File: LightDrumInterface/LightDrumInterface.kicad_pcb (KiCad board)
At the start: 2 copper layers, 151 x 83 mm, 62 parts, among them J1 Conn_01x04_Male, J2 DEBUG-CONN, J3 Conn_01x04_Male, J4 B24B-PHDSS(LF)(SN), J5 B24B-PHDSS(LF)(SN), SW1 RESET-SW, U1 STP16CP05, U2 TPL0401B-10-Q1, U3 74AUP2G04, U4 PC817

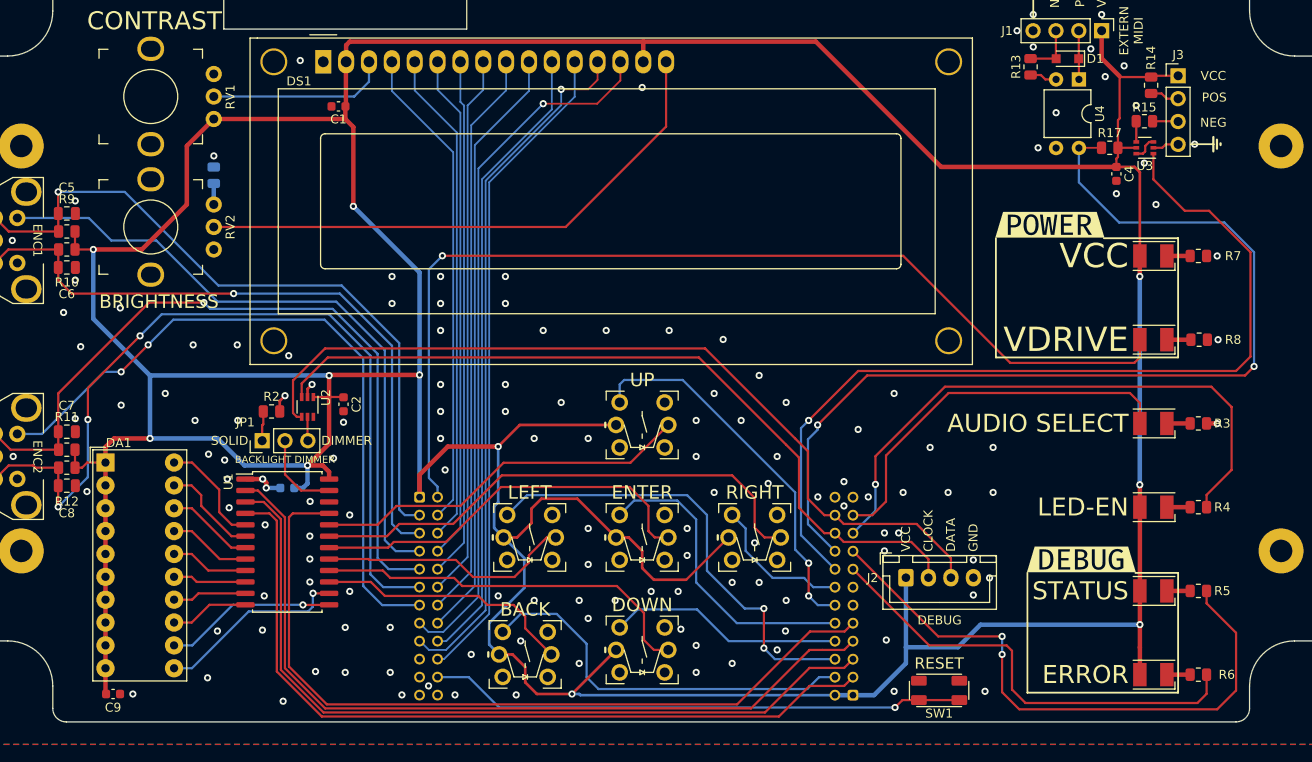
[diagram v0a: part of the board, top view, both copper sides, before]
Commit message: Replace interface harnesses with FPC cable
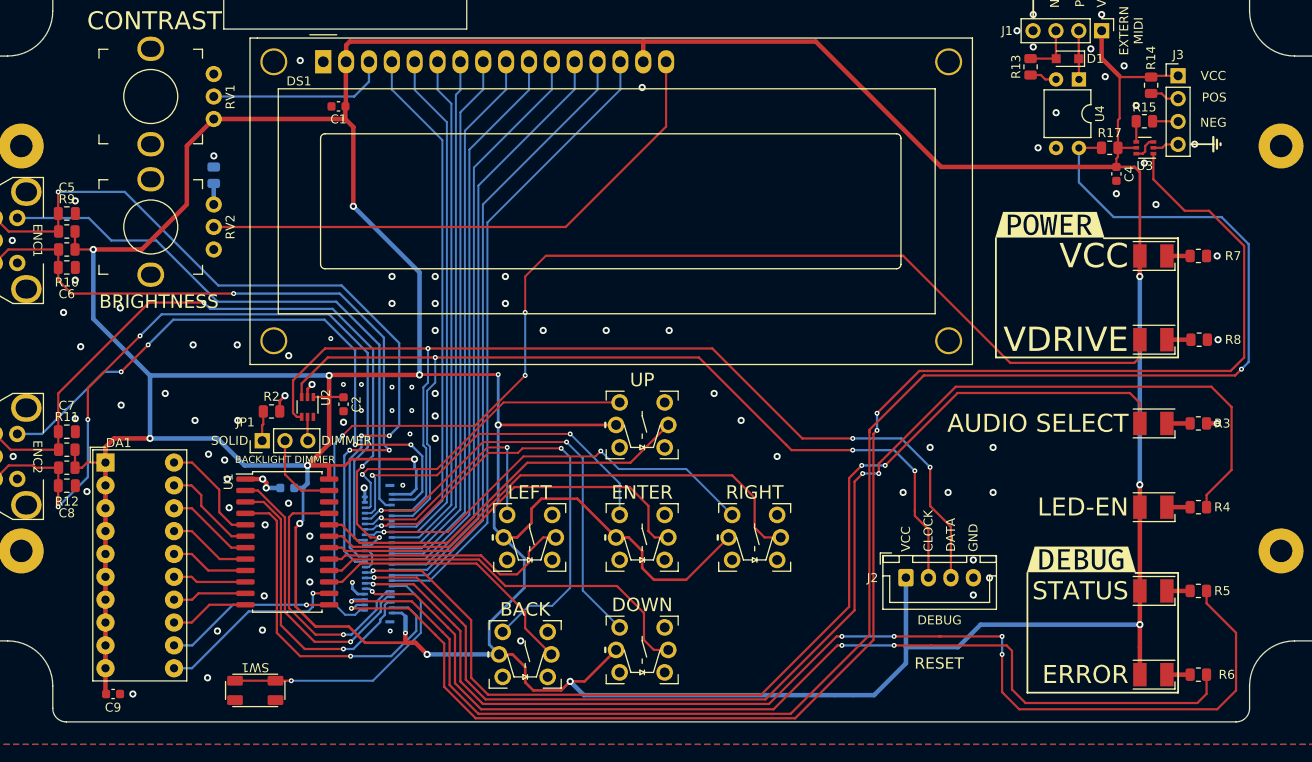
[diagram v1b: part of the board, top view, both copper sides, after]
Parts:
- removed J4, J5: B24B-PHDSS(LF)(SN), Daxxn_Connectors:B24B-PHDSS(LF)(SN)
- added J-INTERFACE1: INTERFACE CONN, Daxxn_Connectors:5025984593, B.Cu at (75.2, 92.8)
- C1, C2, C3, C4, C5, C6, C7, C8: value ${D-CAP} -> 100nF
- R1: value 120${R} -> 120Ω
- R10, R11, R12, R17, R9: value ${P-RES} -> 10KΩ
- R13, R14, R15: value 220${R} -> 220Ω
- R2: value 500${R} -> 560Ω
- R3, R4, R6: value ${LED-RES} -> 330Ω
- R5: value ${LED-RES} -> 470Ω
- R7: value 510${R} -> 3KΩ
- R8: value 1K${R} -> 5.6KΩ
- RV1: value 10K${R} -> 10KΩ
- RV2: value 1K${R} -> 1KΩ
- moved SW1 76.0 mm to (60.0, 108.0), turned to 180 degrees
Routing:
- net /DIAG-AUDIO-SEL: track 43.2 -> 120.7 mm, vias 0 -> 3
- net /DIAG-STRIP-EN: track 65.6 -> 142.0 mm, vias 1 -> 3
- net /MIDI-IN: track 108.6 -> 180.1 mm
- net /MIDI-OUT: track 99.1 -> 168.4 mm, vias 1 -> 3
- net /DIAG-DEBUG: track 50.5 -> 112.9 mm, vias 0 -> 3
- net /DIAG-STATUS: track 66.8 -> 129.0 mm, vias 2 -> 5
- net /IND-~{OE}: track 89.4 -> 29.9 mm, vias 0 -> 1
- net /IND-SDATA: track 90.5 -> 32.0 mm, vias 0 -> 1
- net /IND-CLK: track 89.5 -> 32.9 mm, vias 0 -> 1
- net /IND-LE: track 88.5 -> 38.8 mm, vias 0 -> 1
- net VCC: track 585.8 -> 635.4 mm, vias 11 -> 16
- net /MENU-RIGHT: track 16.2 -> 47.6 mm, vias 0 -> 2
- net /~{RESET}: track 59.7 -> 30.4 mm
- net /MENU-LEFT: track 51.1 -> 27.0 mm
- net /I2C-SCLK: track 87.0 -> 109.9 mm, vias 0 -> 3
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
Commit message: Add docs and gerbers for REV7
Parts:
- H4: value M2.5 -> locked
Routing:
- net Vdrive: track 133.6 -> 123.1 mm
- net /I2C-SDA: track 117.0 -> 119.4 mm
- net /MIDI-IN: track 180.1 -> 178.3 mm
- net /DIAG-AUDIO-SEL: track 120.7 -> 121.6 mm
- net /DIAG-STRIP-EN: track 142.0 -> 142.8 mm
- net /MIDI-OUT: track 168.4 -> 168.2 mm, vias 3 -> 1
- net GND: vias 93 -> 95

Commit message: Add logo to interface PCB
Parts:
- added G***: LOGO, Daxxn_Logos_Art:LightDrum_Logo2_Cu_Spoke, F.Cu at (132.5, 89.5)
- added G***: LOGO, Daxxn_Logos_Art:LightDrum_Logo2, F.Cu at (132.5, 89.5)
- moved J2 9.89 mm to (128.8, 104.7)
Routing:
- net /I2C-SDA: track 119.4 -> 129.3 mm
- net /DIAG-STATUS: track 129.0 -> 119.2 mm, vias 5 -> 3
- net /I2C-SCLK: track 110.0 -> 119.5 mm
- net /MIDI-IN: track 178.3 -> 187.4 mm
- net /MIDI-OUT: track 168.2 -> 177.2 mm
- net /DIAG-STRIP-EN: track 142.8 -> 150.7 mm
- net /DIAG-AUDIO-SEL: track 121.6 -> 129.4 mm
- net /DIAG-DEBUG: track 112.7 -> 107.5 mm
- net VCC: track 635.3 -> 632.7 mm
- net /MENU-LEFT: track 27.0 -> 25.6 mm
- net GND: vias 95 -> 114
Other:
- board text added: "LIGHT DRUM"
- board text added: "REV7"

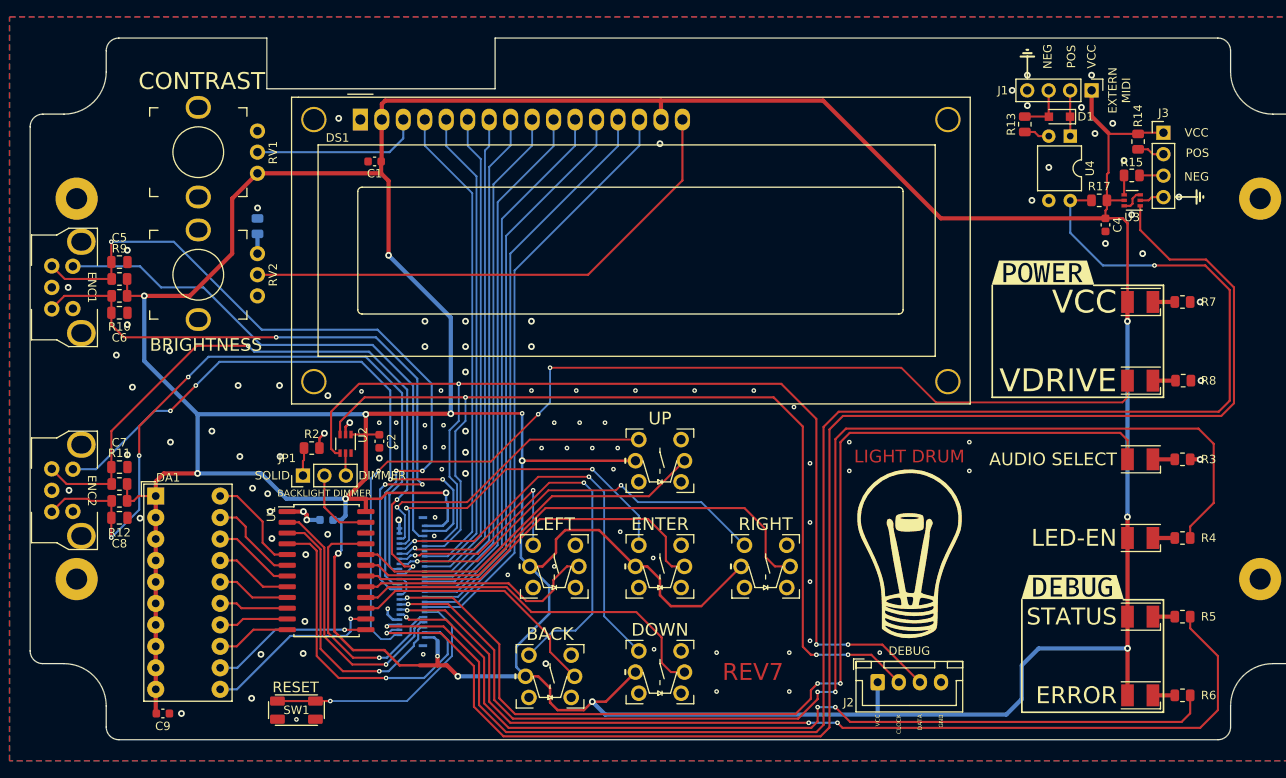
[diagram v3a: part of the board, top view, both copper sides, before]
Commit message: Replaced display and FPC cable
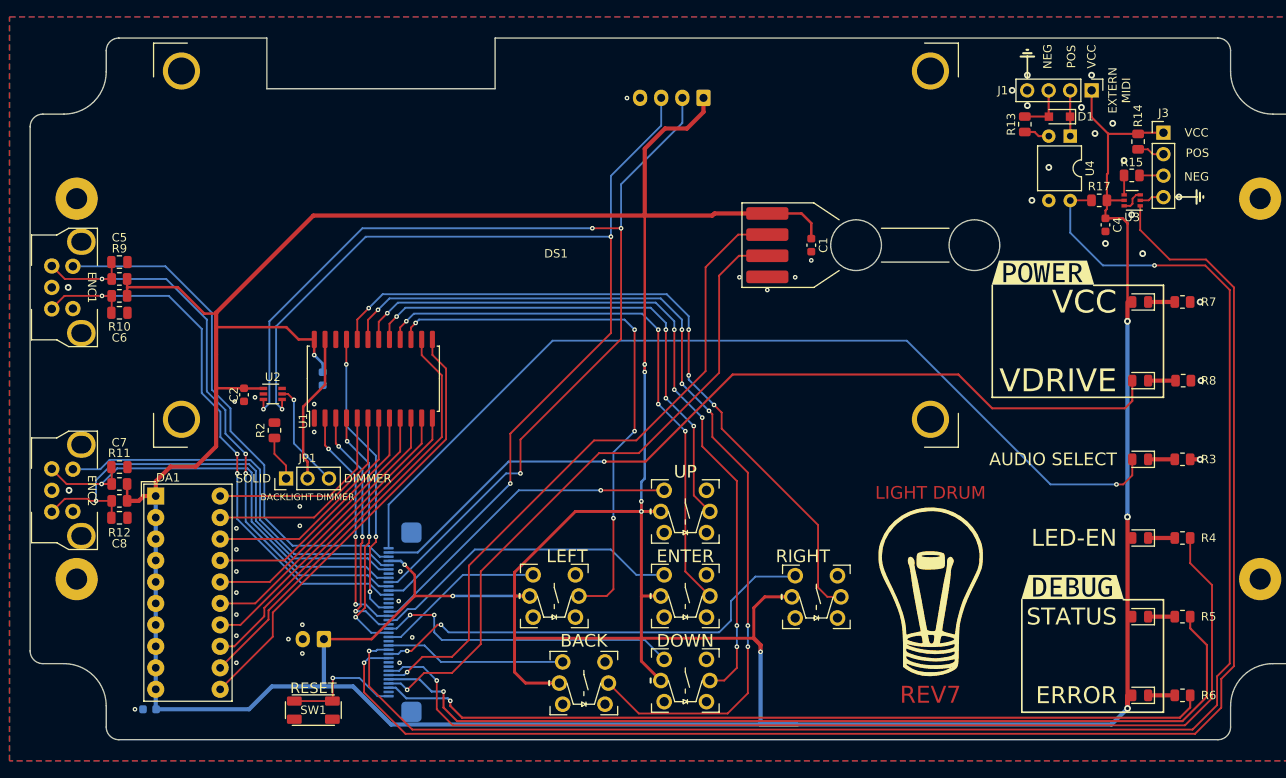
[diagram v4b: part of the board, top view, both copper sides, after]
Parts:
- removed J-INTERFACE1: INTERFACE CONN, Daxxn_Connectors:5025984593
- removed R1: 120Ω, Resistor_SMD:R_0805_2012Metric
- removed RV1: 10KΩ, Daxxn_Switches:PT01-D120K2-B103
- removed RV2: 1KΩ, Daxxn_Switches:PT01-D120K2-B103
- added J4: PWR-CONN, Connector_JST:JST_XA_B02B-XASK-1_1x02_P2.50mm_Vertical, B.Cu at (63.2, 99.6)
- added J6: 0541323662, Daxxn_Connectors:0541323662, B.Cu at (70.9, 97.6)
- C9, J2: moved to B.Cu
- D-AUDIO-SEL1, D-DBG1, D-STA1, D-STRIP-EN1, D-VCC1, D-VDRIVE1: footprint Daxxn_LEDs:LED_PLCC-2 -> LED_SMD:LED_0805_2012Metric
- DS1: value WC1602A -> NX4024T032; footprint Display:WC1602A -> Daxxn_Displays:NX4024T032_10mm_Harness
- moved J2 72.1 mm to (108.2, 35.6), turned to 180 degrees
- moved C1 52.6 mm to (120.9, 53.0), turned to -90 degrees
- moved DS1 27.5 mm to (90.7, 53.0), turned to -90 degrees
- moved U1 23.4 mm to (69.1, 68.8), turned to 90 degrees
- moved C2 16.9 mm to (53.8, 70.7)
- moved C3 16.7 mm to (63.1, 68.8), turned to -90 degrees
- moved U2 10.4 mm to (57.2, 70.6), turned to 0 degrees
- moved S-RGT1 7.00 mm to (121.5, 94.6)
- moved S-UP1 6.71 mm to (106.0, 84.5)
- moved G*** 5.15 mm to (135.0, 94.0) (x2)
- moved R2 4.88 mm to (57.4, 74.9), turned to 90 degrees
- moved S-ACT1 4.61 mm to (106.0, 94.5)
- moved S-BCK1 4.08 mm to (94.0, 104.8)
- moved S-LFT1 3.50 mm to (90.5, 94.5)
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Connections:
- net /I2C-SCLK renamed I2C-SCLK
- net /I2C-SDA renamed I2C-SDA
- D-AUDIO-SEL1 pad 2: /DIAG-AUDIO-SEL -> /AUDIO-RELAY
- DA1 pad 11: Net-(DA1-Pad11) -> Net-(U1-Pad13)
- DA1 pad 12: Net-(DA1-Pad12) -> Net-(U1-Pad14)
- DS1 pad 1: GND -> VCC
- DS1 pad 2: VCC -> /SCR-TX
- DS1 pad 3: Net-(DS1-Pad3) -> /SCR-RX
- DS1 pad 4: /SCR-RS -> GND
- R4 pad 2: /DIAG-STRIP-EN -> /STRIP-PWR
- S-ACT1 pad 6: Net-(S-ACT1-Pad6) -> Net-(U1-Pad16)
- S-BCK1 pad 6: Net-(S-BCK1-Pad6) -> Net-(U1-Pad19)
- S-DWN1 pad 6: Net-(S-DWN1-Pad6) -> Net-(U1-Pad18)
- S-RGT1 pad 6: Net-(S-RGT1-Pad6) -> Net-(U1-Pad20)
- S-UP1 pad 6: Net-(S-UP1-Pad6) -> Net-(U1-Pad17)
- SW1 pad 2: /~{RESET} -> ~{RESET}
- U1 pad 13: Net-(DA1-Pad12) -> Net-(U1-Pad13)
- U1 pad 14: Net-(DA1-Pad11) -> Net-(U1-Pad14)
- U1 pad 15: Net-(S-BCK1-Pad6) -> Net-(S-LFT1-Pad6)
- U1 pad 16: Net-(S-DWN1-Pad6) -> Net-(U1-Pad16)
- U1 pad 17: Net-(S-LFT1-Pad6) -> Net-(U1-Pad17)
- U1 pad 18: Net-(S-ACT1-Pad6) -> Net-(U1-Pad18)
- U1 pad 19: Net-(S-RGT1-Pad6) -> Net-(U1-Pad19)
- U1 pad 2: /IND-SDATA -> /GRAPH-SDI
- U1 pad 20: Net-(S-UP1-Pad6) -> Net-(U1-Pad20)
- U1 pad 21: /IND-~{OE} -> /GRAPH-~{OE}
- U1 pad 3: /IND-CLK -> /GRAPH-CLK
- U1 pad 4: /IND-LE -> /GRAPH-LE
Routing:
- net /DIAG-STRIP-EN: track 150.7 -> 0.00 mm, vias 3 -> 0
- net /DIAG-AUDIO-SEL: track 129.4 -> 0.00 mm, vias 3 -> 0
- net /STRIP-PWR: track 0.00 -> 123.8 mm, vias 0 -> 1
- net /AUDIO-RELAY: track 0.00 -> 110.5 mm, vias 0 -> 1
- net Net-(U1-Pad19): track 0.00 -> 108.0 mm, vias 0 -> 6
- net Net-(U1-Pad18): track 0.00 -> 86.8 mm, vias 0 -> 6
- net Net-(U1-Pad20): track 0.00 -> 85.5 mm, vias 0 -> 4
- net /SCR-TX: track 0.00 -> 78.7 mm, vias 0 -> 1
- net /SCR-RX: track 0.00 -> 78.2 mm, vias 0 -> 1
- net /SCR-D7: track 70.7 -> 0.00 mm
- net /SCR-D6: track 68.9 -> 0.00 mm
- net Net-(U1-Pad16): track 0.00 -> 67.4 mm, vias 0 -> 4
- net /SCR-D5: track 67.2 -> 0.00 mm
- net /SCR-D4: track 65.5 -> 0.00 mm
- net /SCR-D3: track 63.8 -> 0.00 mm
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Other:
- board text removed: "BRIGHTNESS"
- board text removed: "CONTRAST"

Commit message: Replace with smaller case (WIP)
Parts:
- removed H1, H2, H3: M2.5, MountingHole:MountingHole_2.5mm_Pad
- removed H4: locked, MountingHole:MountingHole_2.5mm_Pad
- removed the REF** at (104.0, 70.0)
- added REF**: LeMotech_Black_ENC-115x90, Daxxn_Enclosures:LeMotech_Black_ENC-115x90, F.Cu at (0.00, 0.00)
- moved R6 220.4 mm to (-6.00, -33.0), turned to -90 degrees
- moved D-DBG1 219.8 mm to (-6.00, -38.0), turned to 90 degrees
- moved R5 208.5 mm to (1.80, -33.0), turned to -90 degrees
- moved D-STA1 207.8 mm to (1.80, -38.0), turned to 90 degrees
- moved R4 196.6 mm to (9.60, -33.0), turned to -90 degrees
- moved D-STRIP-EN1 195.8 mm to (9.60, -38.0), turned to 90 degrees
- moved kibuzzard-62EEA0C0 189.5 mm to (5.50, -27.0)
- moved R3 184.7 mm to (17.4, -33.0), turned to -90 degrees
- moved D-AUDIO-SEL1 183.9 mm to (17.4, -38.0), turned to 90 degrees
- moved G*** 176.6 mm to (-30.0, 31.0) (x2)
- moved R8 172.9 mm to (25.2, -32.9), turned to -90 degrees
- moved D-VDRIVE1 172.0 mm to (25.2, -38.0), turned to 90 degrees
- moved C9 162.4 mm to (-33.5, -35.5), turned to -90 degrees
- moved R7 161.2 mm to (33.0, -33.0), turned to -90 degrees
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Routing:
- net VCC: track 584.7 -> 0.00 mm, vias 11 -> 0
- net /MIDI-IN: track 187.9 -> 0.00 mm, vias 2 -> 0
- net /MIDI-OUT: track 178.4 -> 0.00 mm, vias 1 -> 0
- net I2C-SCLK: track 131.3 -> 0.00 mm, vias 4 -> 0
- net I2C-SDA: track 127.9 -> 0.00 mm, vias 3 -> 0
- net /STRIP-PWR: track 123.8 -> 0.00 mm, vias 1 -> 0
- net /DIAG-STATUS: track 111.4 -> 0.00 mm, vias 1 -> 0
- net /AUDIO-RELAY: track 110.5 -> 0.00 mm, vias 1 -> 0
- net Net-(U1-Pad19): track 108.0 -> 0.00 mm, vias 6 -> 0
- net Vdrive: track 101.1 -> 0.00 mm, vias 1 -> 0
- net /DIAG-DEBUG: track 98.6 -> 0.00 mm, vias 1 -> 0
- net Net-(U1-Pad18): track 86.8 -> 0.00 mm, vias 6 -> 0
- net Net-(U1-Pad20): track 85.5 -> 0.00 mm, vias 4 -> 0
- net /SCR-TX: track 78.7 -> 0.00 mm, vias 1 -> 0
- net /SCR-RX: track 78.2 -> 0.00 mm, vias 1 -> 0
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- removed copper zone on B.Cu, net GND
- removed copper zone on F.Cu, net GND
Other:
- board size 151 x 83 mm -> 108 x 83 mm
- board text added: "REV8"
- board text removed: "REV7"

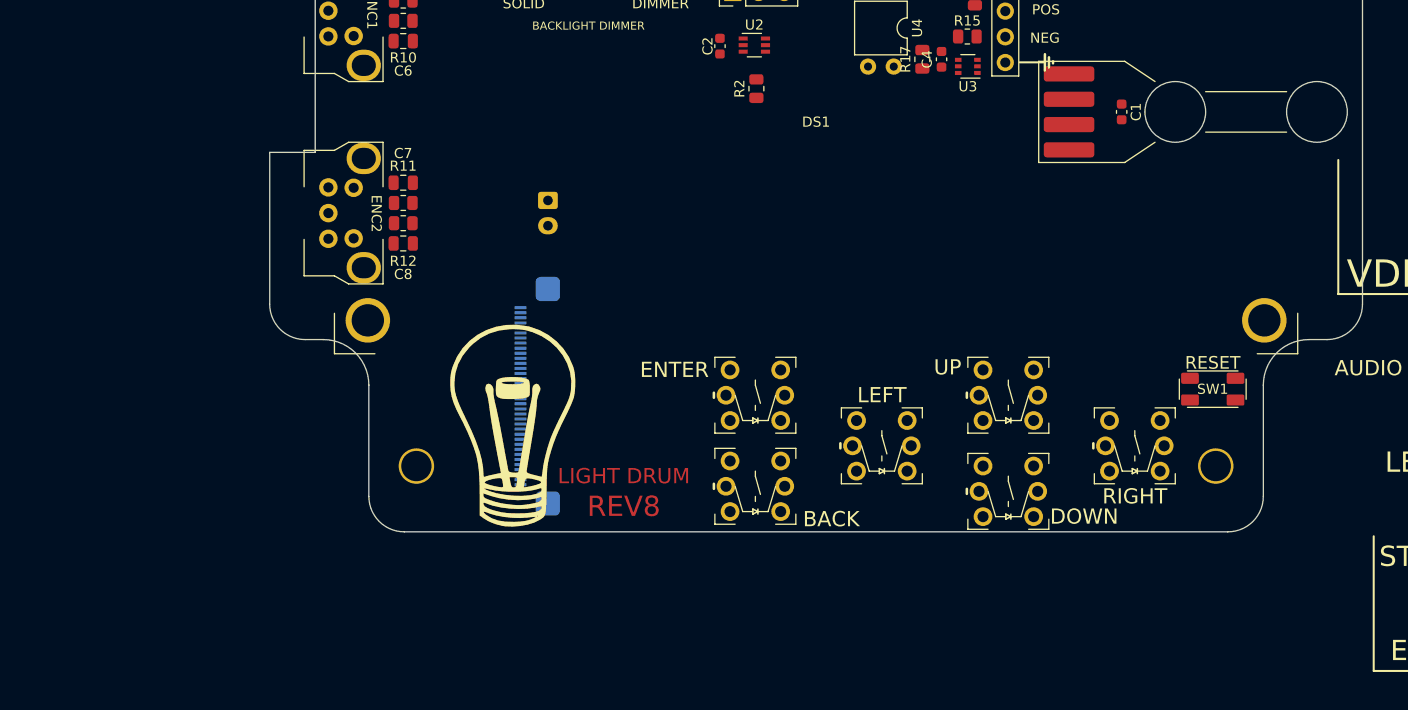
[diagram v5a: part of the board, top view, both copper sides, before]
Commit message: Simplify analog power supply and add some routing
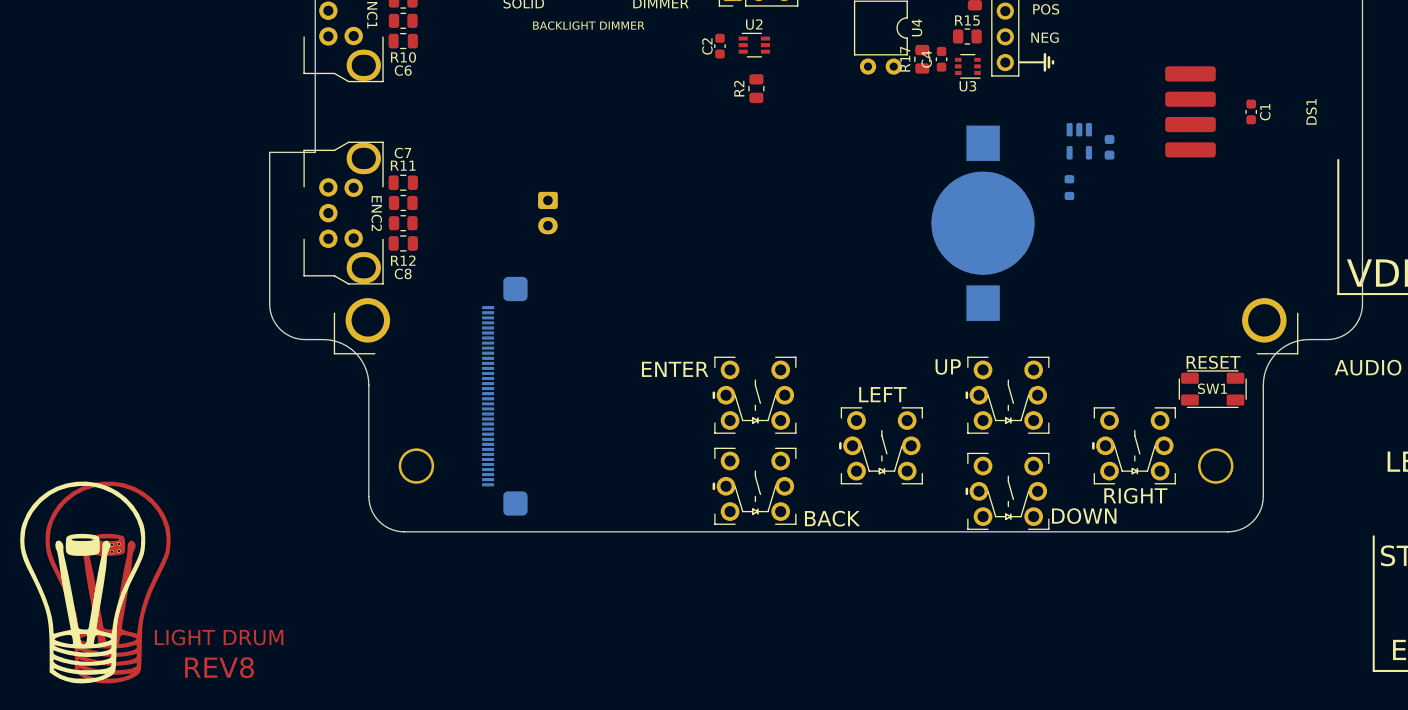
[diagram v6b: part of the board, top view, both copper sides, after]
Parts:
- added BAT101: 12mm COIN, Battery:BatteryHolder_Keystone_3000_1x12mm, B.Cu at (16.5, 11.0)
- added C101: 100nF, Capacitor_SMD:C_0603_1608Metric, B.Cu at (29.0, 3.50)
- added R101: 1.2K, Resistor_SMD:R_0603_1608Metric, B.Cu at (25.0, 7.48)
- added U101: LTC4054ES5-4.2, Package_TO_SOT_SMD:TSOT-23-5, B.Cu at (26.0, 2.90)
- DS1: footprint Daxxn_Displays:NX4024T032_10mm_Harness -> Daxxn_Displays:NX4024T032_10mm
- moved G*** 45.2 mm to (-72.5, 46.5)
- moved G*** 42.9 mm to (-70.0, 46.5)
- moved C1 12.8 mm to (43.0, 0.00)
- moved J6 3.20 mm to (-32.4, 28.1)
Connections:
- C2 pad 1: VCC -> VDD
- C3 pad 1: VCC -> VDD
- C9 pad 1: VCC -> VDD
- D-DBG1 pad 2: VCC -> VDD
- D-STA1 pad 2: VCC -> VDD
- D-STRIP-EN1 pad 2: VCC -> VDD
- D-VCC1 pad 2: VCC -> VDD
- DA1 pad 1: VCC -> VDD
- DA1 pad 10: VCC -> VDD
- DA1 pad 2: VCC -> VDD
- DA1 pad 3: VCC -> VDD
- DA1 pad 4: VCC -> VDD
- DA1 pad 5: VCC -> VDD
- DA1 pad 6: VCC -> VDD
- DA1 pad 7: VCC -> VDD
- DA1 pad 8: VCC -> VDD
- DA1 pad 9: VCC -> VDD
- J6 pad 13: GND -> VCC
- J6 pad 14: GND -> /VBAT
- J6 pad 23: GND -> /CHARGE-STATUS
- J6 pad 35: GND -> VDD
- J6 pad 4: VCC -> VDD
- R10 pad 1: VCC -> VDD
- R11 pad 2: VCC -> VDD
- R12 pad 1: VCC -> VDD
- R9 pad 2: VCC -> VDD
- S-ACT1 pad 5: VCC -> VDD
- S-BCK1 pad 5: VCC -> VDD
- S-DWN1 pad 5: VCC -> VDD
- S-LFT1 pad 5: VCC -> VDD
- S-RGT1 pad 5: VCC -> VDD
- S-UP1 pad 5: VCC -> VDD
- U1 pad 24: VCC -> VDD
- U2 pad 1: VCC -> VDD
